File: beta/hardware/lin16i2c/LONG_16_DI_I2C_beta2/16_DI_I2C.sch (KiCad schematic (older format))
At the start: 84 parts, among them K1 CONN_3, K2 CONN_3, P1 CONN_2, P10 CONN_5, P11 CONN_3X2, P12 CONN_5, P13 CONN_2, P2 CONN_2, P3 CONN_2, P4 CONN_2, P5 CONN_2, P6 CONN_2, P7 CONN_2, P8 CONN_2, P9 CONN_3X2, U1 PCF8574, U2 PCF8574

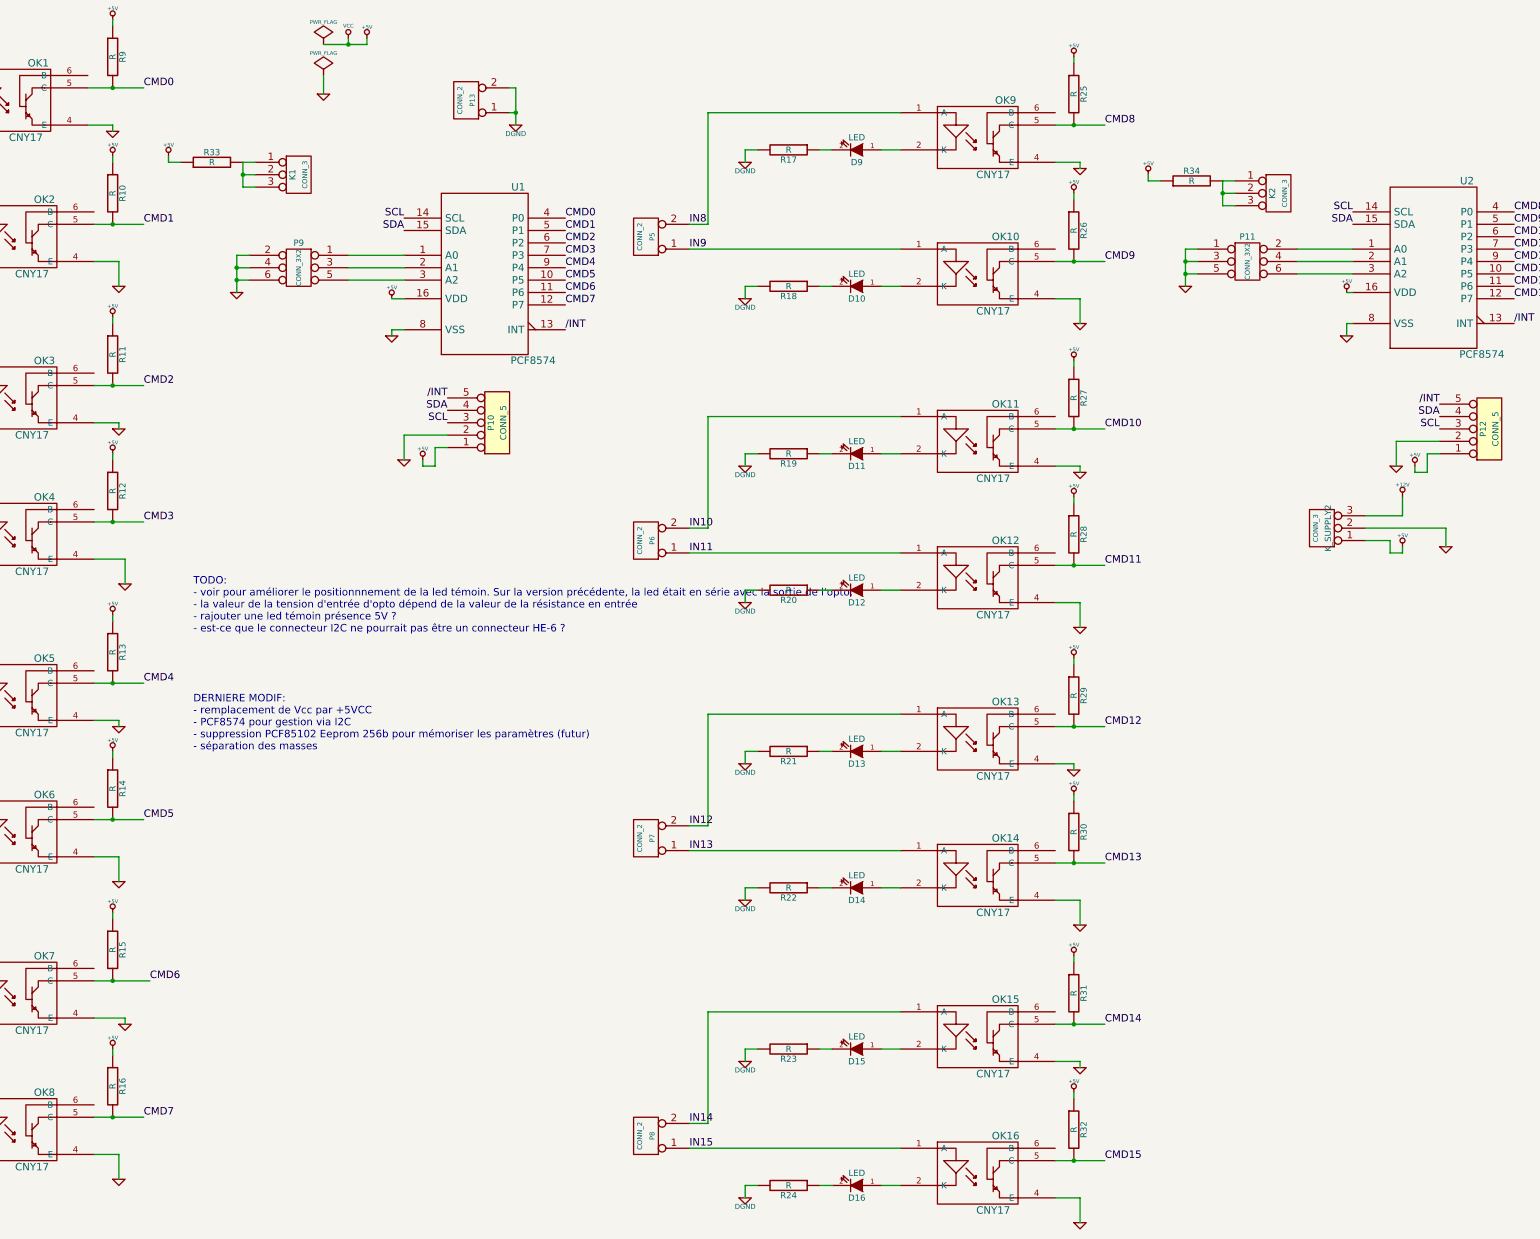
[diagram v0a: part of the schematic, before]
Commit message: Modification groupe de pin d'adressage i2c Placement des composants pour validation Suppression K_Supply2
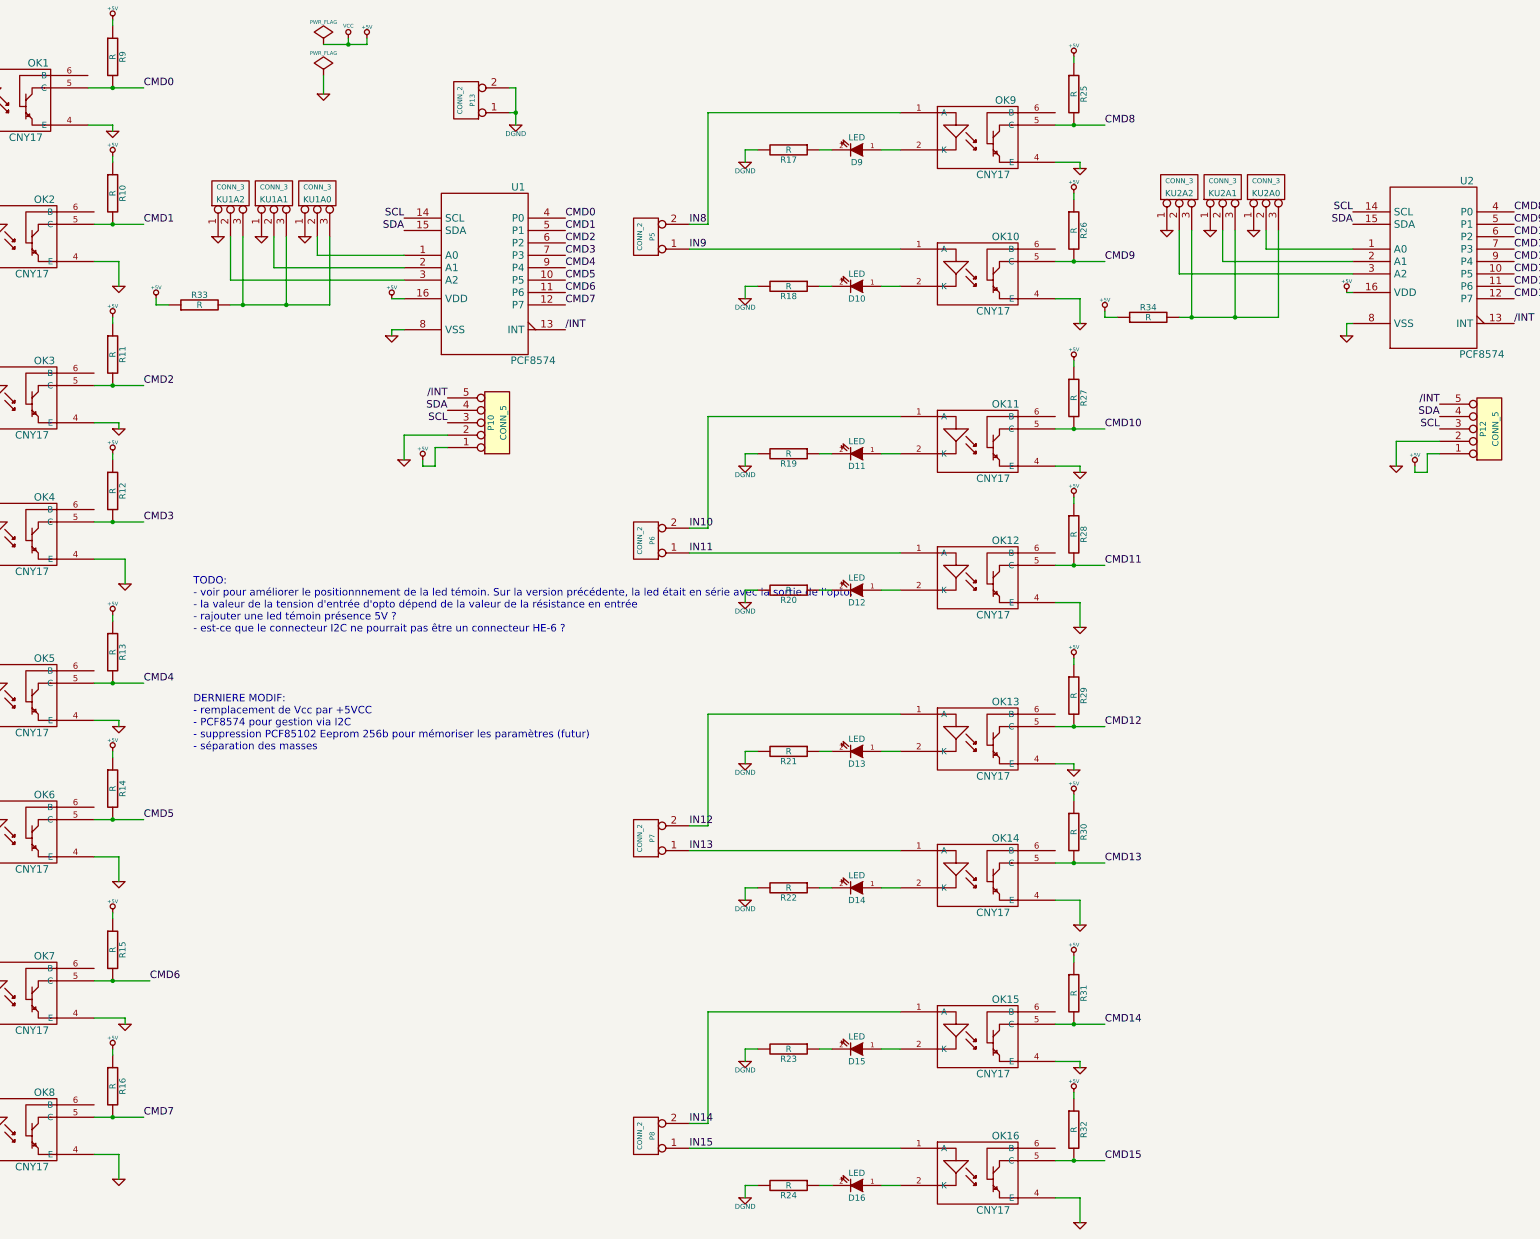
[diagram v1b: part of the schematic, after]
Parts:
- removed K1, K2, K_SUPPLY2: CONN_3, symbol CONN_3
- removed P11, P9: CONN_3X2, symbol CONN_3X2
- added KU1A0, KU1A1, KU1A2, KU2A0, KU2A1, KU2A2: CONN_3, symbol CONN_3
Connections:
- net GND: now also KU1A0.1 (P1), KU1A1.1 (P1), KU1A2.1 (P1), KU2A0.1 (P1), KU2A1.1 (P1), KU2A2.1 (P1)
- net at U1.1 (A0): now also KU1A0.2 (PM)
- net at U1.2 (A1): now also KU1A1.2 (PM)
- net at U1.3 (A2): now also KU1A2.2 (PM)
- net at U2.1 (A0): now also KU2A0.2 (PM)
- net at U2.2 (A1): now also KU2A1.2 (PM)
- net at U2.3 (A2): now also KU2A2.2 (PM)
- net at R33.2: now also KU1A0.3 (P3), KU1A1.3 (P3), KU1A2.3 (P3)
- net at R34.2: now also KU2A0.3 (P3), KU2A1.3 (P3), KU2A2.3 (P3)
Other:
- moved on the sheet: R33, R34

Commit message: routage
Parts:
- added R35, R36, R37, R38: R, symbol R
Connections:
- net +5V: now also R35.1, R36.1, R37.1, R38.1
- net at KU1A2.3 (P3), R33.2: no longer KU1A0.3 (P3), KU1A1.3 (P3)
- new net: KU1A0.3 (P3), R35.2
- new net: KU1A1.3 (P3), R34.2
- new net: KU2A1.3 (P3), R37.2
- new net: KU2A0.3 (P3), R38.2
- new net: KU2A2.3 (P3), R36.2
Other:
- moved on the sheet: R33
